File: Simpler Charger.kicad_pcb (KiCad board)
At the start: 4 copper layers, 54.5 x 44 mm, 33 parts, among them J1 POWER, J2 PORT_A, J3 PORT_B, U1 TPS25858-Q1

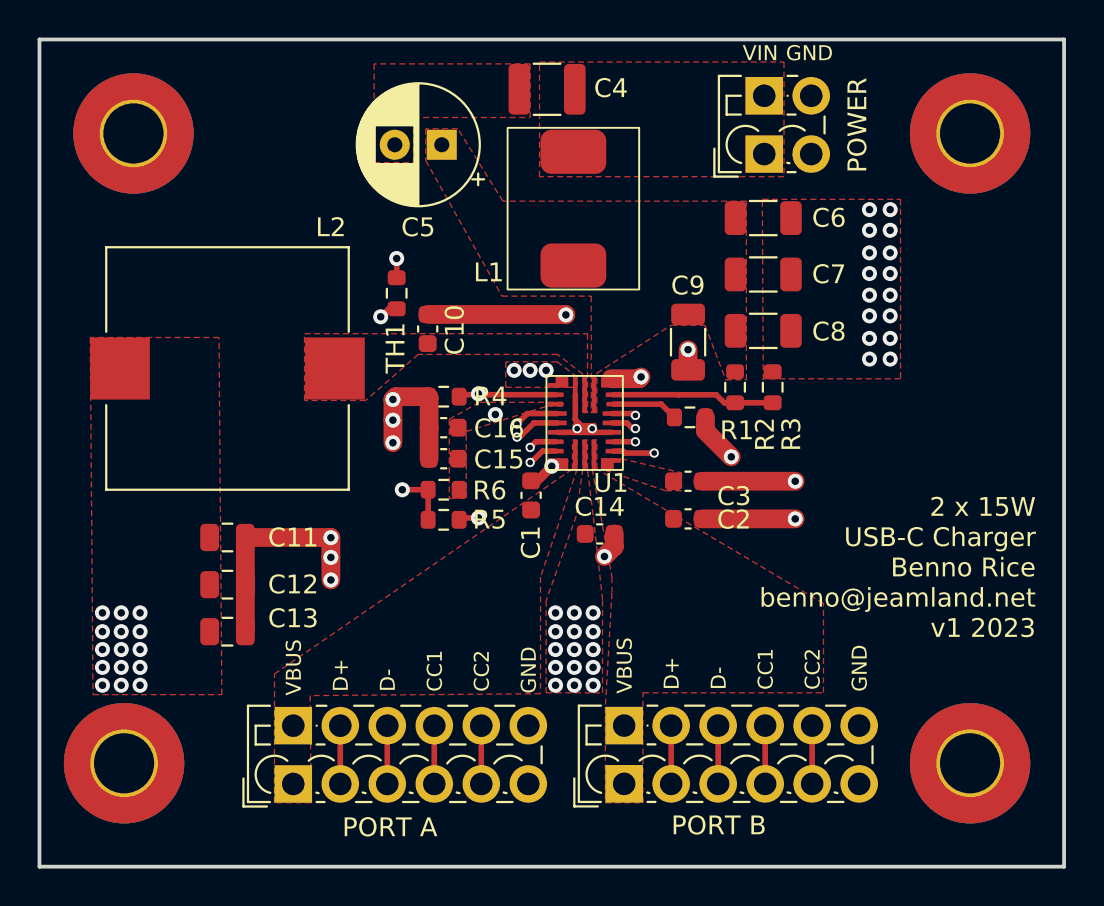
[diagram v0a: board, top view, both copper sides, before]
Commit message: Move things around so L2's loop is shorter
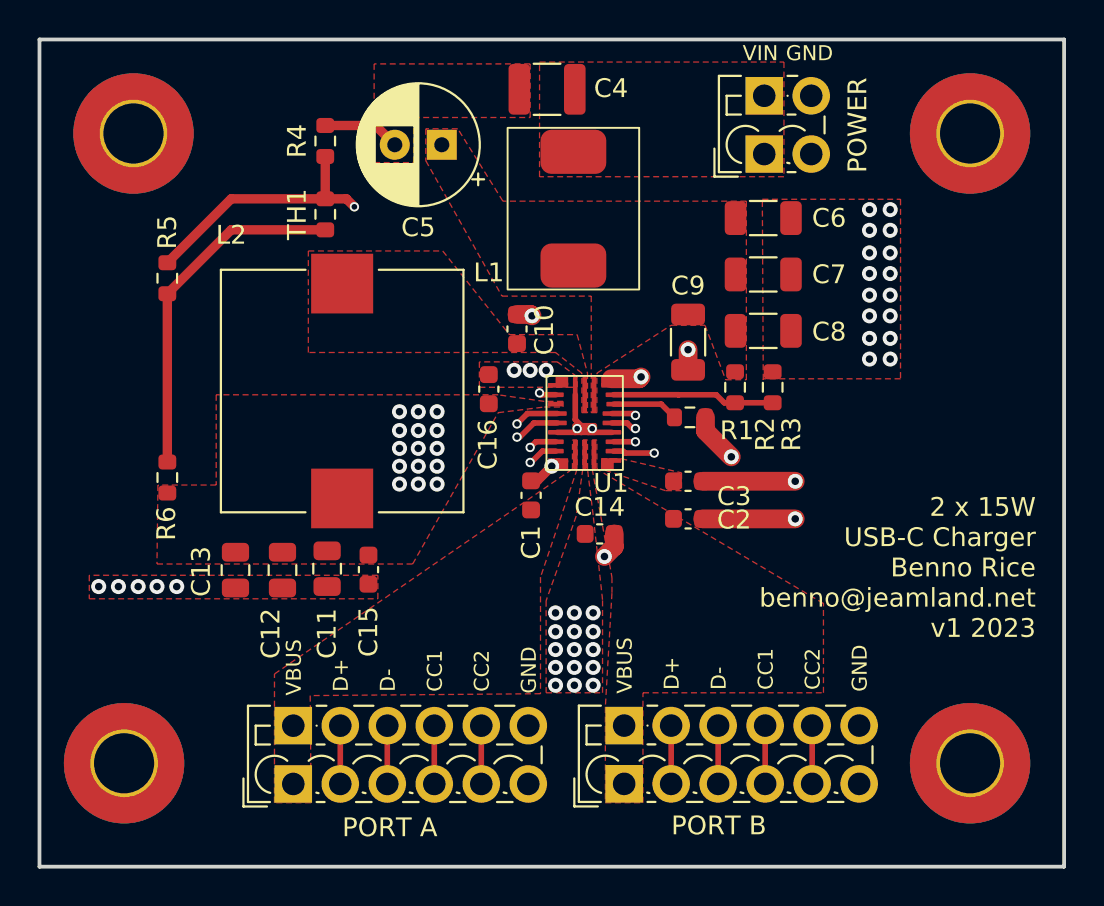
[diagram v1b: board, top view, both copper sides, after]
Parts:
- moved R5 19.5 mm to (117.8, 57.2), turned to 90 degrees
- moved R4 15.0 mm to (126.2, 49.9), turned to 90 degrees
- moved R6 14.7 mm to (117.8, 67.8), turned to -90 degrees
- moved C15 7.13 mm to (128.5, 72.7), turned to -90 degrees
- moved L2 6.22 mm to (127.1, 63.2), turned to -90 degrees
- moved TH1 5.66 mm to (126.2, 53.8), turned to 90 degrees
- moved C11 5.55 mm to (126.3, 72.7), turned to -90 degrees
- moved C10 4.75 mm to (136.4, 59.9)
- moved C13 3.30 mm to (121.4, 72.7), turned to -90 degrees
- moved C16 3.16 mm to (134.9, 63.1), turned to 90 degrees
- moved C12 3.03 mm to (123.9, 72.7), turned to -90 degrees
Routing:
- net GND: track 41.9 -> 26.7 mm, vias 33 -> 32
- net /BIAS: track 10.6 -> 0.00 mm, vias 31 -> 30
- net /TS: track 21.3 -> 29.5 mm, vias 3 -> 2
- net Net-(U1-BOOT): track 14.4 -> 9.60 mm
- net Net-(R5-Pad1): track 17.7 -> 18.8 mm, vias 2 -> 0

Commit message: Hopefully better thermals for the high-current bits
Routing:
- net Net-(U1-BOOT): track 9.60 -> 0.00 mm, vias 2 -> 8
- net Net-(U1-SW): vias 0 -> 4
- net Net-(U1-IN): vias 0 -> 4
- net Net-(J1-Pin_1): vias 0 -> 4
- net /VBUS_B: vias 0 -> 4
- net /VBUS_A: vias 0 -> 4
- net /BIAS: vias 30 -> 34
- added copper zone on B.Cu, net /BIAS
- added copper zone on B.Cu, net /VBUS_A
- added copper zone on B.Cu, net /VBUS_B
- added copper zone on In1.Cu, net GND
- added copper zone on In2.Cu, net GND
- added copper zone on B.Cu, net Net-(J1-Pin_1)
- added copper zone on B.Cu, net Net-(U1-BOOT)
- added copper zone on F.Cu, net Net-(U1-BOOT)
- added copper zone on B.Cu, net Net-(U1-IN)
- added copper zone on B.Cu, net Net-(U1-SW)
- removed copper zone on In1.Cu, net /BIAS

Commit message: Adjust silkscreen text sizes, put mounting holes in paste layer
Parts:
- moved C12 0.58 mm to (123.3, 72.8)
- moved C13 0.58 mm to (120.8, 72.8)

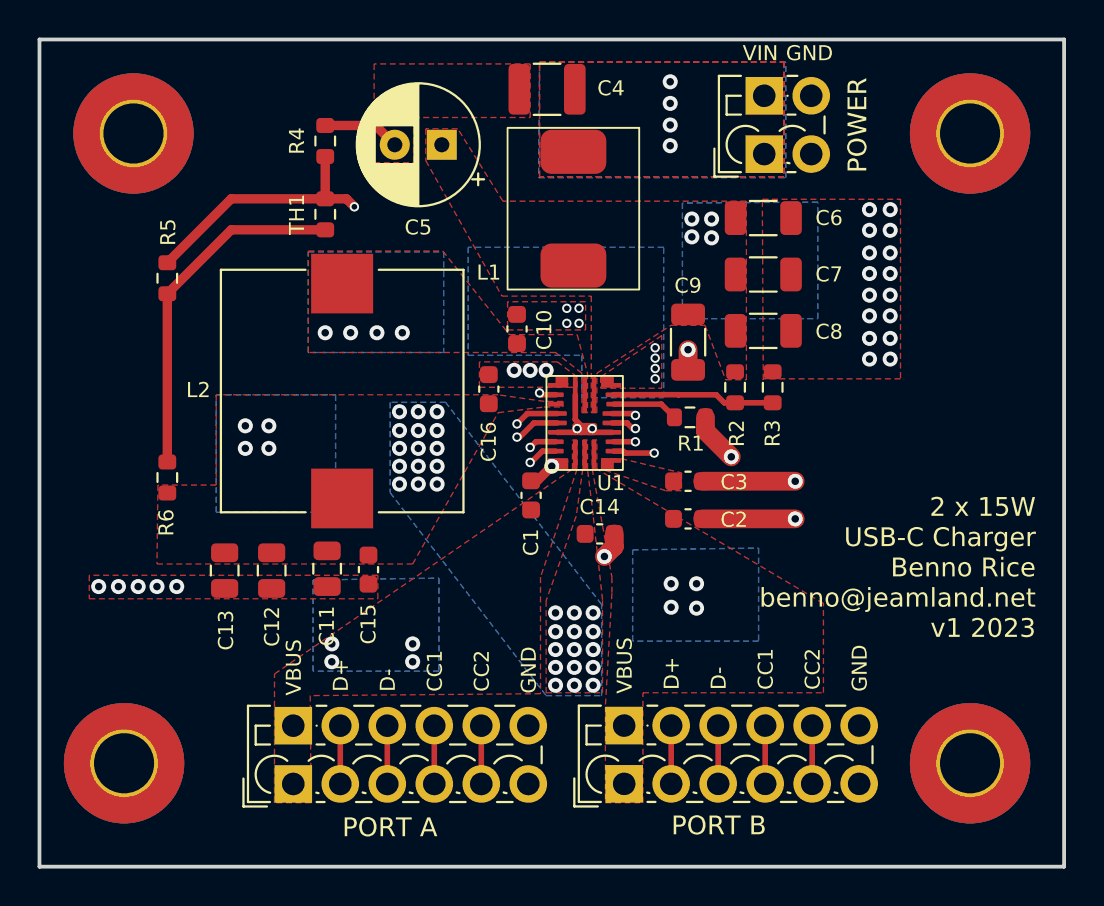
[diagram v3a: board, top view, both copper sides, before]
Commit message: Round corners, shuffle some silkscreens
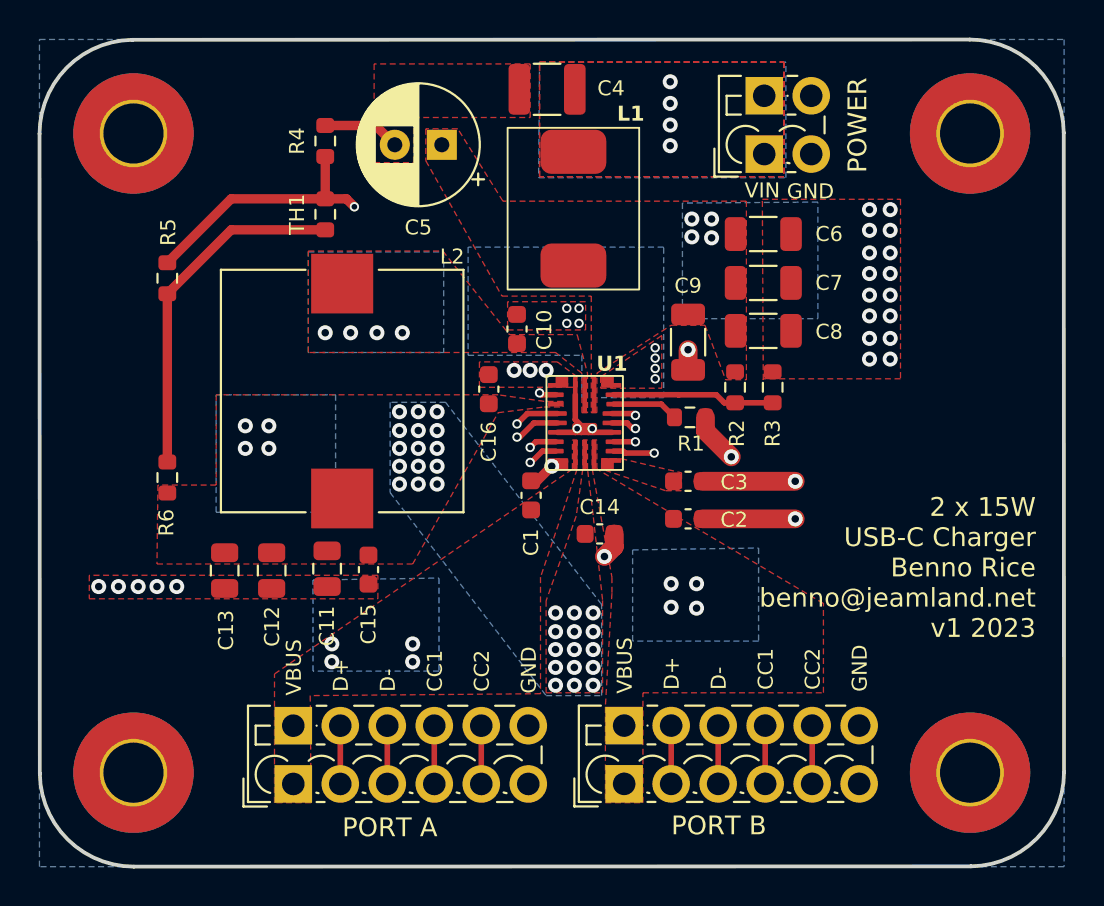
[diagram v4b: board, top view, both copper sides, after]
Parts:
- moved C6 0.85 mm to (149.5, 54.9)
- moved H3 0.71 mm to (116.0, 83.5)
- moved H4 0.50 mm to (160.5, 83.5)
- moved C7 0.45 mm to (149.5, 57.5)
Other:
- outline, holes or cut-outs redrawn
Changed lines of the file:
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@@
     (property "ki_keywords" "inductor choke coil reactor magnetic")
     (attr smd)
-    (fp_text reference "L2" (at -0.05 7.65 180) (layer "F.SilkS")
+    (fp_text reference "L2" (at -7.15 -5.85 180) (layer "F.SilkS")
         (effects (font (size 0.8 0.8) (thickness 0.15)))
     )
@@
   )
   (footprint "MountingHole:MountingHole_3.2mm_M3_Pad_TopBottom" (layer "F.Cu")
-    (at 160.5 83)
+    (at 160.5 83.5)
     (descr "Mounting Hole 3.2mm, M3")
     (tags "mounting hole 3.2mm m3")
@@
     (property "ki_keywords" "inductor choke coil reactor magnetic")
     (attr smd)
-    (fp_text reference "L1" (at 3.4 4.5 unlocked) (layer "F.SilkS")
-        (effects (font (size 0.8 0.8) (thickness 0.1)))
+    (fp_text reference "L1" (at -5.05 -3.05 unlocked) (layer "F.SilkS")
+        (effects (font (size 0.8 0.8) (thickness 0.15) bold))
     )
     (fp_text value "1µH" (at 0 1 -90 unlocked) (layer "F.Fab")
@@
   )
   (footprint "Capacitor_SMD:C_1206_3216Metric" (layer "F.Cu")
-    (at 149.5 57)
+    (at 149.5 57.45)
     (descr "Capacitor SMD 1206 (3216 Metric), square (rectangular) end terminal, IPC_7351 nominal, (Body size source: IPC-SM-782 page 76, https://www.pcb-3d.com/wordpress/wp-content/uploads/ipc-sm-782a_amendment_1_and_2.pdf), generated with kicad-footprint-generator")
     (tags "capacitor")
@@
   )
   (footprint "Capacitor_SMD:C_1206_3216Metric" (layer "F.Cu")
-    (at 149.5 54)
+    (at 149.5 54.85)
     (descr "Capacitor SMD 1206 (3216 Metric), square (rectangular) end terminal, IPC_7351 nominal, (Body size source: IPC-SM-782 page 76, https://www.pcb-3d.com/wordpress/wp-content/uploads/ipc-sm-782a_amendment_1_and_2.pdf), generated with kicad-footprint-generator")
     (tags "capacitor")
@@
     (property "Type" "SMD")
     (attr smd)
-    (fp_text reference "U1" (at 1.4 3.203003 unlocked) (layer "F.SilkS")
-        (effects (font (size 0.8 0.8) (thickness 0.1)))
+    (fp_text reference "U1" (at 1.45 -3.146997 unlocked) (layer "F.SilkS")
+        (effects (font (size 0.8 0.8) (thickness 0.15) bold))
     )
     (fp_text value "TPS25858-Q1" (at 0 1 unlocked) (layer "F.Fab")
@@
   )
   (footprint "MountingHole:MountingHole_3.2mm_M3_Pad_TopBottom" (layer "F.Cu")
-    (at 115.5 83)
+    (at 116 83.5)
     (descr "Mounting Hole 3.2mm, M3")
     (tags "mounting hole 3.2mm m3")
@@
     )
   )
-  (gr_rect (start 111 44.5) (end 165.5 88.5)
-    (stroke (width 0.2) (type default)) (fill none) (layer "Edge.Cuts"))
+  (gr_line (start 111.017989 83.546656) (end 111.003095 49.517988)
+    (stroke (width 0.2) (type default)) (layer "Edge.Cuts"))
+  (gr_line (start 160.546656 88.482011) (end 116.017988 88.496905)
+    (stroke (width 0.2) (type default)) (layer "Edge.Cuts"))
+  (gr_arc (start 116.017988 88.496905) (mid 112.5 87.05) (end 111.017989 83.546656)
+    (stroke (width 0.2) (type default)) (layer "Edge.Cuts"))
+  (gr_arc (start 111.003095 49.517988) (mid 112.45 46) (end 115.953344 44.517989)
+    (stroke (width 0.2) (type default)) (layer "Edge.Cuts"))
+  (gr_line (start 115.953344 44.517989) (end 160.482012 44.503095)
+    (stroke (width 0.2) (type default)) (layer "Edge.Cuts"))
+  (gr_arc (start 160.482012 44.503095) (mid 164 45.95) (end 165.482011 49.453344)
+    (stroke (width 0.2) (type default)) (layer "Edge.Cuts"))
+  (gr_arc (start 165.496905 83.482012) (mid 164.05 87) (end 160.546656 88.482011)
+    (stroke (width 0.2) (type default)) (layer "Edge.Cuts"))
+  (gr_line (start 165.482011 49.453344) (end 165.496905 83.482012)
+    (stroke (width 0.2) (type default)) (layer "Edge.Cuts"))
   (gr_text "CC2" (at 135 79.2 90) (layer "F.SilkS")
     (effects (font (size 0.8 0.8) (thickness 0.125)) (justify left bottom))
@@
     (effects (font (size 0.8 0.8) (thickness 0.125)) (justify left bottom))
   )
-  (gr_text "VIN" (at 148.4 45.7) (layer "F.SilkS")
+  (gr_text "VIN" (at 148.5 53) (layer "F.SilkS")
     (effects (font (size 0.8 0.8) (thickness 0.15)) (justify left bottom))
   )
@@
     (effects (font (size 0.8 0.8) (thickness 0.125)) (justify left bottom))
   )
-  (gr_text "GND" (at 150.7 45.7) (layer "F.SilkS")
+  (gr_text "GND" (at 150.75 53.05) (layer "F.SilkS")
     (effects (font (size 0.8 0.8) (thickness 0.15)) (justify left bottom))
   )
